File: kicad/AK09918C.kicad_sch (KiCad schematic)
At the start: 2 parts, among them U601 AK09918

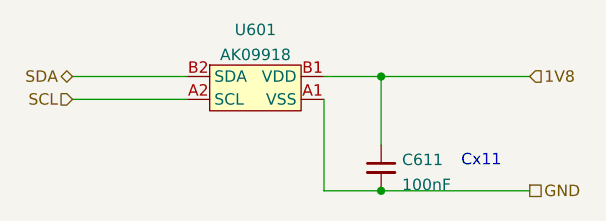
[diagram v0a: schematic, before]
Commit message: Broke down sensor block into a tree of sheets
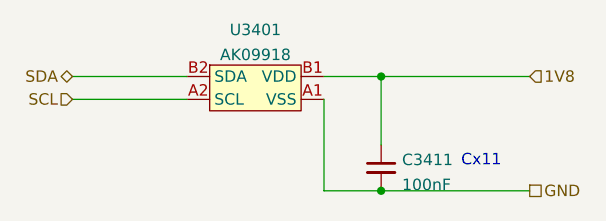
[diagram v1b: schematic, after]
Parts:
- renumbered C611 to C3411, U601 to U3401
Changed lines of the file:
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@@
   (symbol (lib_id "KwanSystems:AK09918") (at 160.02 91.44 0)
     (in_bom yes) (on_board yes) (fields_autoplaced)
-    (property "Reference" "U601" (id 0) (at 160.02 83.7143 0))
+    (property "Reference" "U3401" (id 0) (at 160.02 83.7143 0))
     (property "Value" "AK09918" (id 1) (at 160.02 86.4894 0))
     (property "Footprint" "KwanSystems:AK09918C" (id 2) (at 160.02 91.44 0)
@@
   (symbol (lib_id "Device:C_Small") (at 173.99 99.06 0)
     (in_bom yes) (on_board yes) (fields_autoplaced)
-    (property "Reference" "C611" (id 0) (at 176.3141 98.1578 0)
+    (property "Reference" "C3411" (id 0) (at 176.3141 98.1578 0)
       (effects (font (size 1.27 1.27)) (justify left))
     )

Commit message: Added Digikey references
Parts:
- C3411: Digikey (none) -> 399-C0402C104K4RAC7411CT-ND
- U3401: Digikey (none) -> 974-1155-1-ND; Purpose (none) -> Magnetic sensor
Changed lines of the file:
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@@
+      (effects (font (size 1.27 1.27)) hide)
+    )
+    (property "Digikey" "974-1155-1-ND" (id 4) (at 160.02 91.44 0)
+      (effects (font (size 1.27 1.27)) hide)
+    )
+    (property "Purpose" "Magnetic sensor" (id 5) (at 160.02 91.44 0)
       (effects (font (size 1.27 1.27)) hide)
     )
@@
       (effects (font (size 1.27 1.27)) hide)
     )
+    (property "Digikey" "399-C0402C104K4RAC7411CT-ND" (id 4) (at 173.99 99.06 0)
+      (effects (font (size 1.27 1.27)) hide)
+    )

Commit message: Added a purpose field to bypass capacitors
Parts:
- C3411: Purpose (none) -> AK bypass
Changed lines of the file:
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@@
+      (effects (font (size 1.27 1.27)) hide)
+    )
+    (property "Purpose" "AK bypass" (id 5) (at 173.99 99.06 0)
       (effects (font (size 1.27 1.27)) hide)
     )

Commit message: Checkin before branch
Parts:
- renumbered C3411 to C1811, U3401 to U1801
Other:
- company: (none) -> Kwan Systems
- title: (none) -> Rollercoasterometer
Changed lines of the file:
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@@
 (kicad_sch (version 20211123) (generator eeschema)
-  (paper "A4")
+  (paper "USLetter")
+  (title_block
+    (title "Rollercoasterometer")
+    (date "2022-10-07")
+    (company "Kwan Systems")
+  )
   (junction (at 173.99 101.6) (diameter 0) (color 0 0 0 0)
   )
@@
     (effects (font (size 1.27 1.27)) (justify left))
   )
-  (symbol (lib_id "KwanSystems:AK09918") (at 160.02 91.44 0)
+  (symbol (lib_id "KwanSystems:AK09918") (at 160.02 91.44 0) (unit 1)
     (in_bom yes) (on_board yes) (fields_autoplaced)
-    (property "Reference" "U3401" (id 0) (at 160.02 83.7143 0))
-    (property "Value" "AK09918" (id 1) (at 160.02 86.4894 0))
+    (property "Reference" "U1801" (id 0) (at 160.02 83.981 0))
+    (property "Value" "AK09918" (id 1) (at 160.02 86.5179 0))
     (property "Footprint" "KwanSystems:AK09918C" (id 2) (at 160.02 91.44 0)
       (effects (font (size 1.27 1.27)) hide)
@@
     (pin "B2")
   )
-  (symbol (lib_id "Device:C_Small") (at 173.99 99.06 0)
+  (symbol (lib_id "Device:C_Small") (at 173.99 99.06 0) (unit 1)
     (in_bom yes) (on_board yes) (fields_autoplaced)
-    (property "Reference" "C3411" (id 0) (at 176.3141 98.1578 0)
+    (property "Reference" "C1811" (id 0) (at 176.3141 98.2316 0)
       (effects (font (size 1.27 1.27)) (justify left))
     )
-    (property "Value" "100nF" (id 1) (at 176.3141 100.9329 0)
+    (property "Value" "100nF" (id 1) (at 176.3141 100.7685 0)
       (effects (font (size 1.27 1.27)) (justify left))
     )
